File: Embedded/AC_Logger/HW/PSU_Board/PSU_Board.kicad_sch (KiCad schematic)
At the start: 6 parts, among them J1 Screw_Terminal_01x02, J2 NS25-W3P male

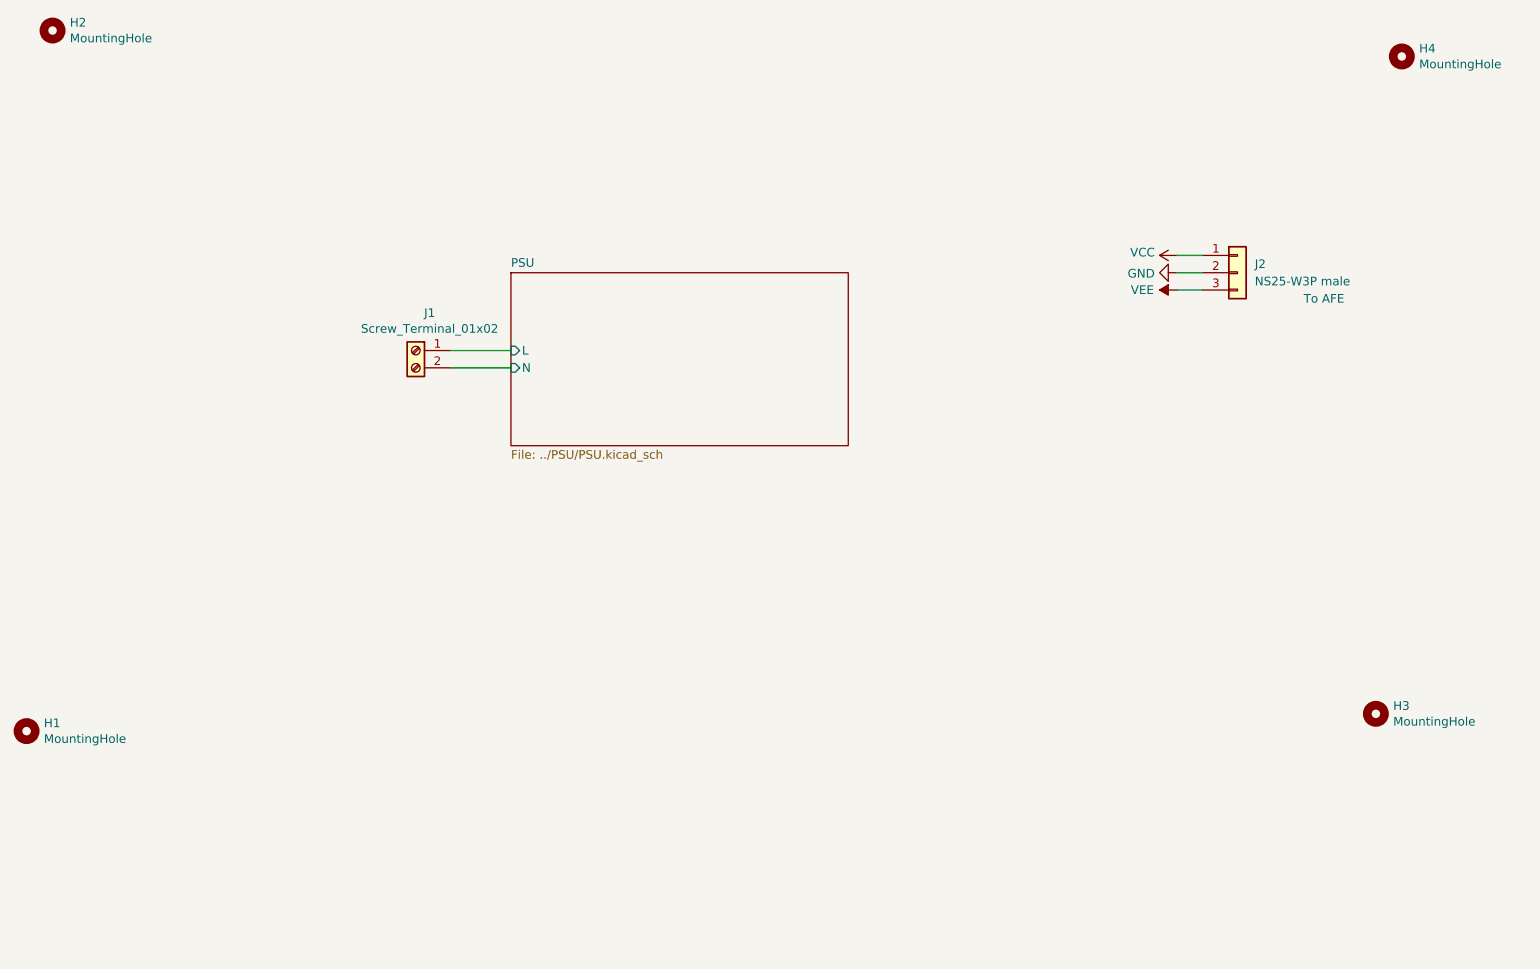
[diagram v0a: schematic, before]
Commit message: PCB changed to make sandwitch.
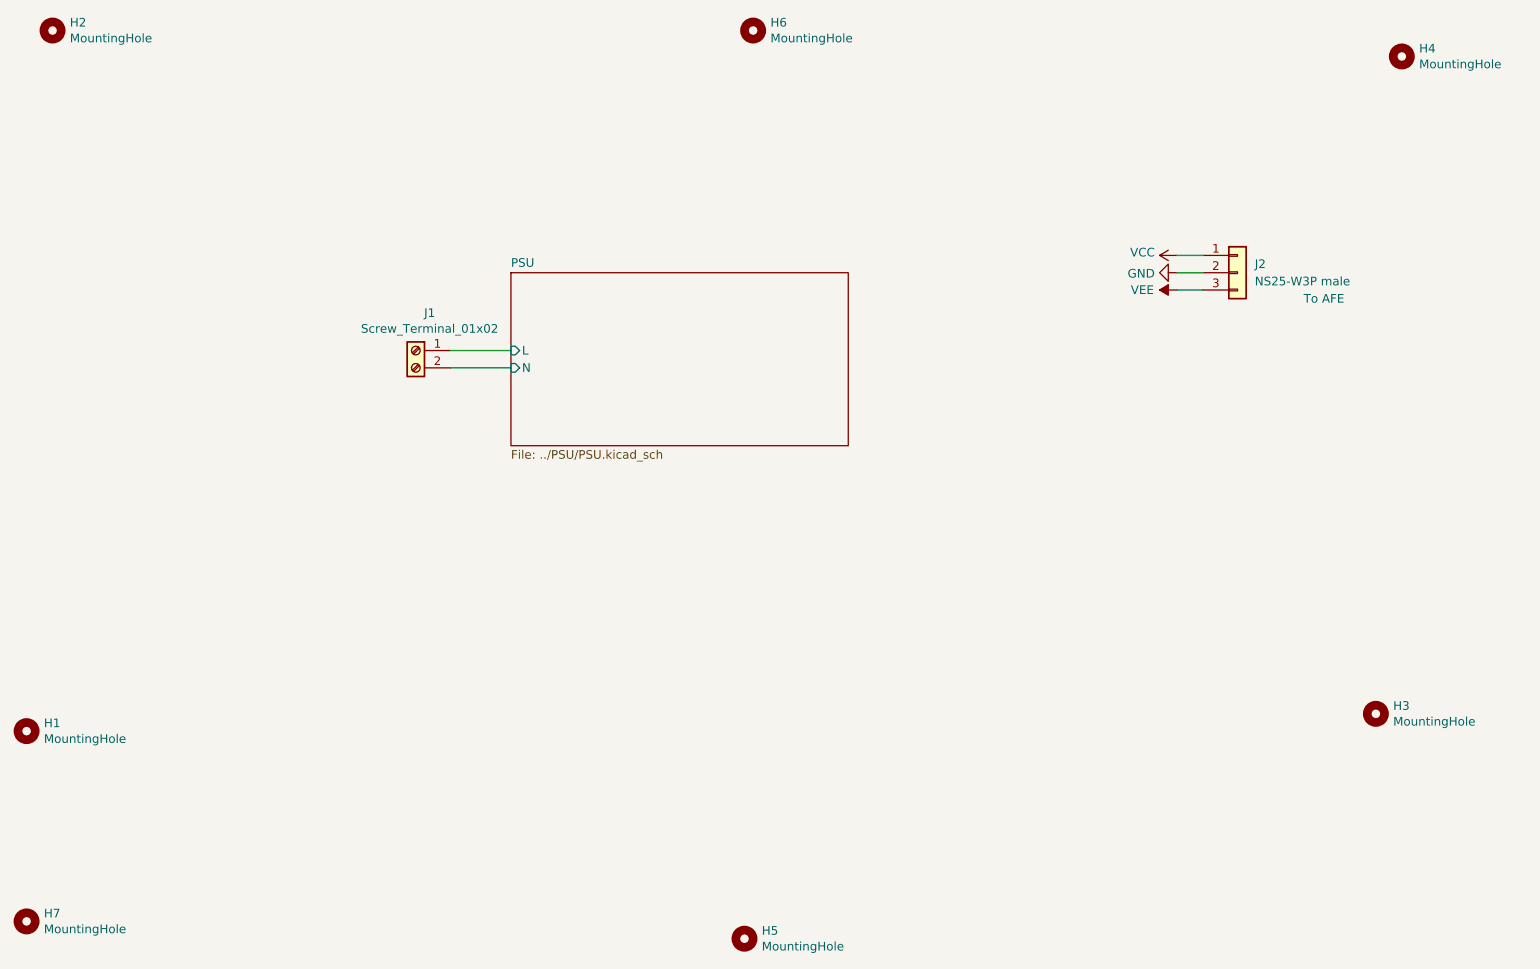
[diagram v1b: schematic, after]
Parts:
- added H5, H6, H7: MountingHole, MountingHole:MountingHole_3.2mm_M3_ISO7380_Pad, symbol Mechanical:MountingHole
